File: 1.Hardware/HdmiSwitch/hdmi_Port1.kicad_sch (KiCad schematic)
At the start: 16 parts

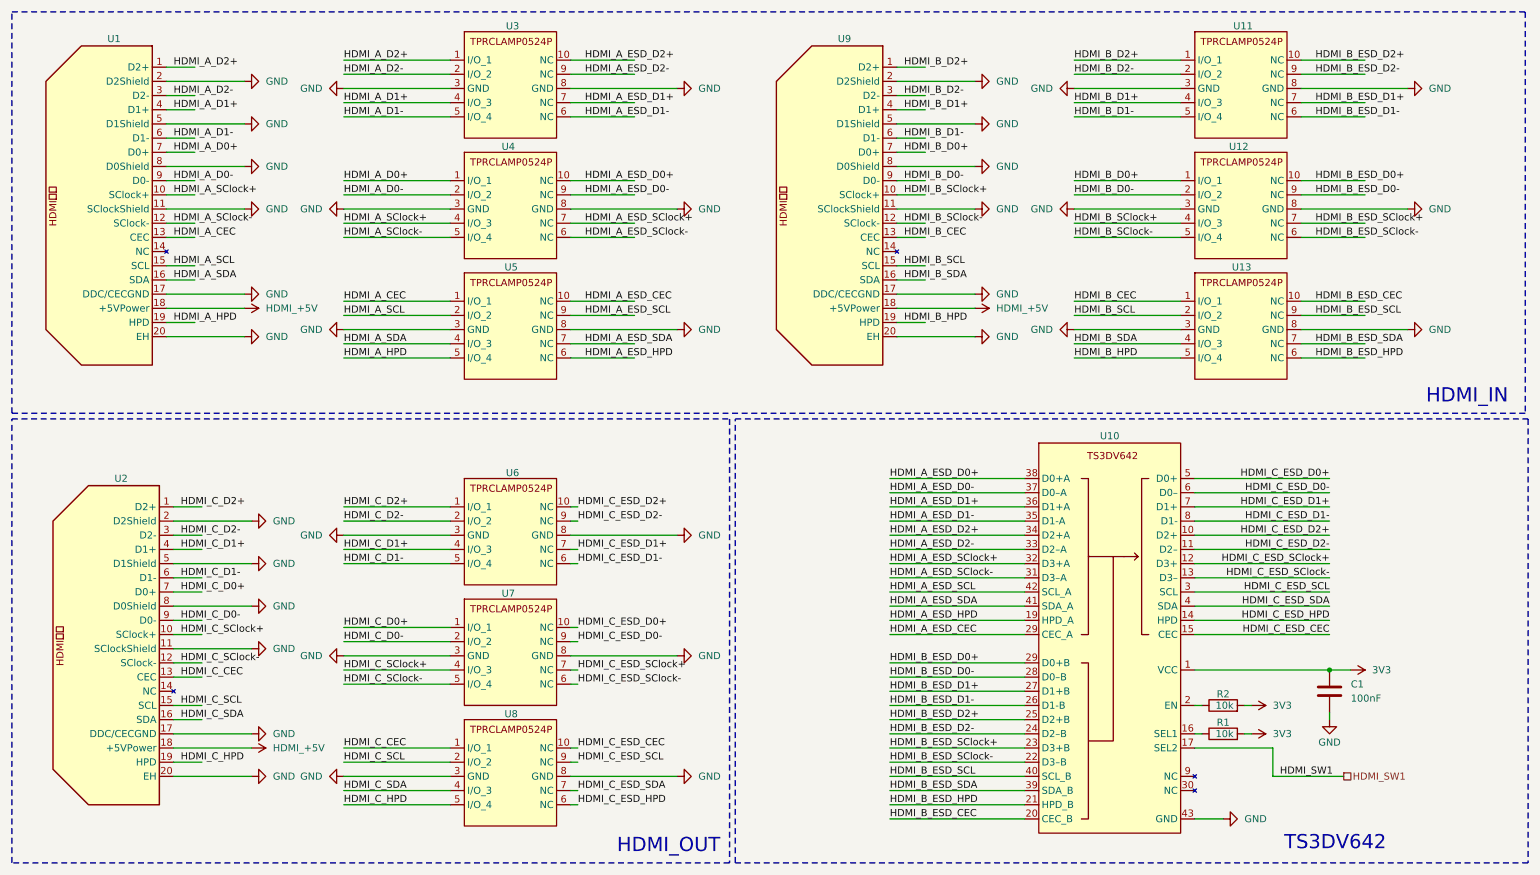
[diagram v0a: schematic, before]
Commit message: 为HDMISwitch模块添加了封装模型
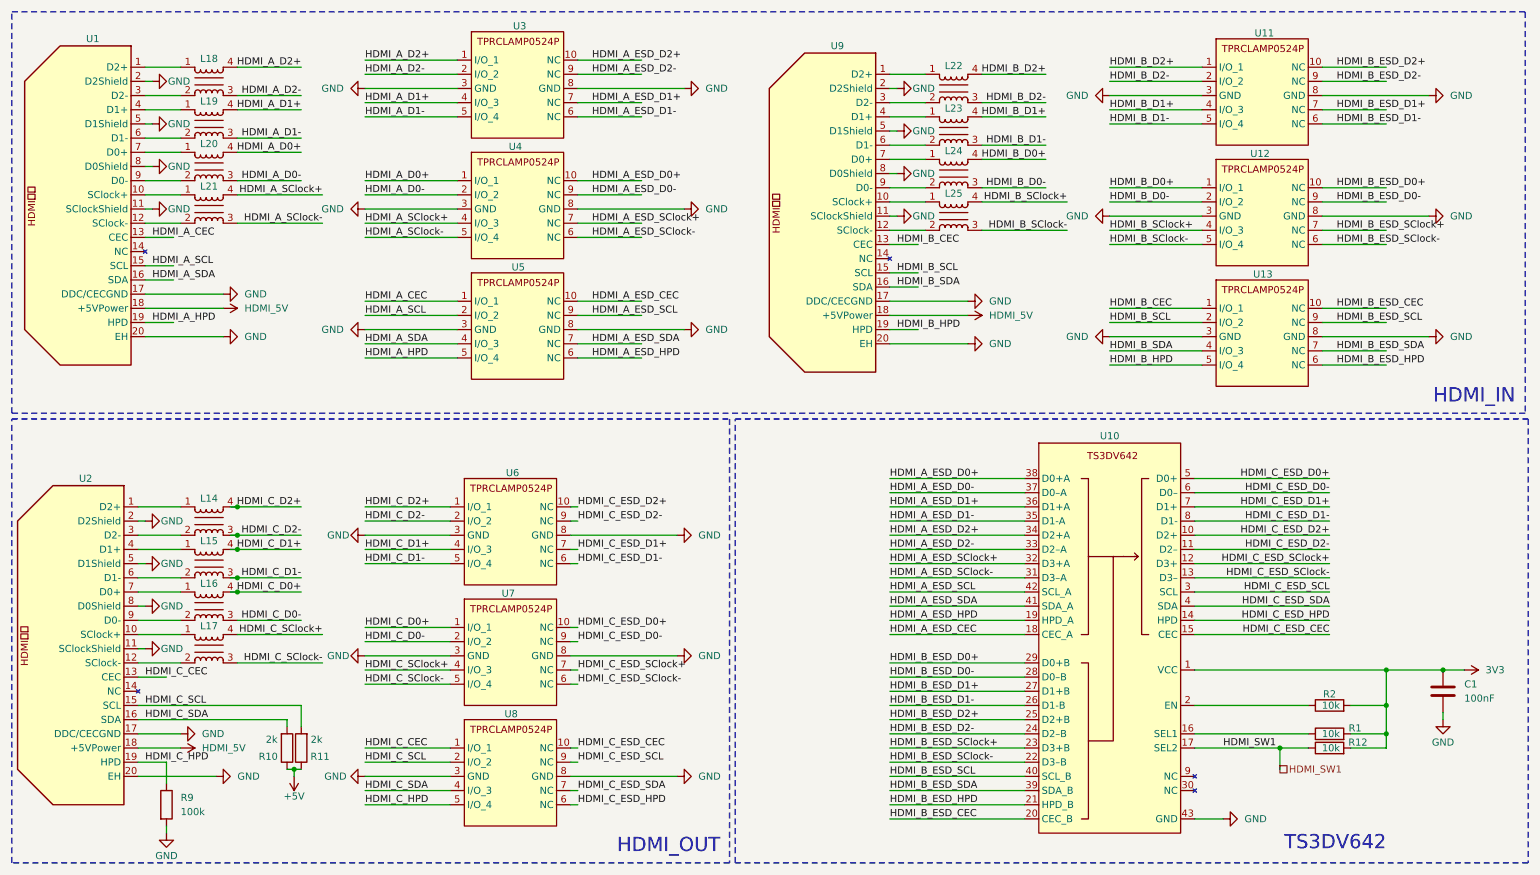
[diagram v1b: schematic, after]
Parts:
- added L14, L15, L16, L17, L18, L19, L20, L21, L22, L23, L24, L25: ~, HdmiSwitch:ACM2012-900-2P-T002, symbol HdmiSwitch:ACM2012-900-2P-T002
- added R10, R11: 2k, Resistor_SMD:R_0402_1005Metric, symbol Device:R
- added R12: 10k, Capacitor_SMD:C_0402_1005Metric, symbol Device:R
- added R9: 100k, Resistor_SMD:R_0402_1005Metric, symbol Device:R
- C1: footprint (none) -> Capacitor_SMD:C_0402_1005Metric
- R1, R2: footprint (none) -> Resistor_SMD:R_0402_1005Metric
- U1, U2, U9: footprint (none) -> HdmiSwitch:HDMI侧插
- U10: footprint (none) -> HdmiSwitch:TS3DV642
- U11, U12, U13, U3, U4, U5, U6, U7, U8: footprint (none) -> HdmiSwitch:TPRCLAMP0524P
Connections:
- net 3V3: now also R12.2
- net GND: now also R9.2
- net HDMI_A_D0+: now also L20.4; no longer U1.7 (D0+)
- net HDMI_A_D0-: now also L20.3; no longer U1.9 (D0-)
- net HDMI_A_D1+: now also L19.4; no longer U1.4 (D1+)
- net HDMI_A_D1-: now also L19.3; no longer U1.6 (D1-)
- net HDMI_A_D2+: now also L18.4; no longer U1.1 (D2+)
- net HDMI_A_D2-: now also L18.3; no longer U1.3 (D2-)
- net HDMI_A_ESD_CEC: now also U10.18 (CEC_A); no longer U10.29 (D0+B)
- net HDMI_A_SClock+: now also L21.4; no longer U1.10 (SClock+)
- net HDMI_A_SClock-: now also L21.3; no longer U1.12 (SClock-)
- net HDMI_B_D0+: now also L24.4; no longer U9.7 (D0+)
- net HDMI_B_D0-: now also L24.3; no longer U9.9 (D0-)
- net HDMI_B_D1+: now also L23.4; no longer U9.4 (D1+)
- net HDMI_B_D1-: now also L23.3; no longer U9.6 (D1-)
- net HDMI_B_D2+: now also L22.4; no longer U9.1 (D2+)
- net HDMI_B_D2-: now also L22.3; no longer U9.3 (D2-)
- net HDMI_B_SClock+: now also L25.4; no longer U9.10 (SClock+)
- net HDMI_B_SClock-: now also L25.3; no longer U9.12 (SClock-)
- net HDMI_C_D0+: now also L16.4; no longer U2.7 (D0+)
- net HDMI_C_D0-: now also L16.3; no longer U2.9 (D0-)
- net HDMI_C_D1+: now also L15.4; no longer U2.4 (D1+)
- net HDMI_C_D1-: now also L15.3; no longer U2.6 (D1-)
- net HDMI_C_D2+: now also L14.4; no longer U2.1 (D2+)
- net HDMI_C_D2-: now also L14.3; no longer U2.3 (D2-)
- net HDMI_C_HPD: now also R9.1
- net HDMI_C_SCL: now also R11.2
- net HDMI_C_SClock+: now also L17.4; no longer U2.10 (SClock+)
- net HDMI_C_SClock-: now also L17.3; no longer U2.12 (SClock-)
- net HDMI_C_SDA: now also R10.2
- net HDMI_SW1: now also R12.1
- net HDMI_+5V renamed HDMI_5V
- new net: L18.1, U1.1 (D2+)
- new net: L21.1, U1.10 (SClock+)
- new net: L21.2, U1.12 (SClock-)
- new net: L18.2, U1.3 (D2-)
- new net: L19.1, U1.4 (D1+)
- new net: L19.2, U1.6 (D1-)
- new net: L20.1, U1.7 (D0+)
- new net: L20.2, U1.9 (D0-)
- new net: L17.1, U2.10 (SClock+)
- new net: L17.2, U2.12 (SClock-)
- new net: L16.1, U2.7 (D0+)
- new net: L16.2, U2.9 (D0-)
- new net: L23.1, U9.4 (D1+)
- new net: L23.2, U9.6 (D1-)
- new net: L25.1, U9.10 (SClock+)
- new net: L25.2, U9.12 (SClock-)
- new net: L22.1, U9.1 (D2+)
- new net: L22.2, U9.3 (D2-)
- new net: L24.1, U9.7 (D0+)
- new net: L24.2, U9.9 (D0-)
- new net: L14.1, U2.1 (D2+)
- new net: L14.2, U2.3 (D2-)
- new net: L15.1, U2.4 (D1+)
- new net: L15.2, U2.6 (D1-)
- new net +5V: R10.1, R11.1
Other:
- moved on the sheet: C1, R1, R2
